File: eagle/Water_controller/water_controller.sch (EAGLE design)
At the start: 50 parts, among them IC1 MAX3232CSE, J1 J12MM, J2 J12MM, J3 J12MM, Q1 IRF740, T1 BT138-V, T2 BT138-V, T3 BT138-V

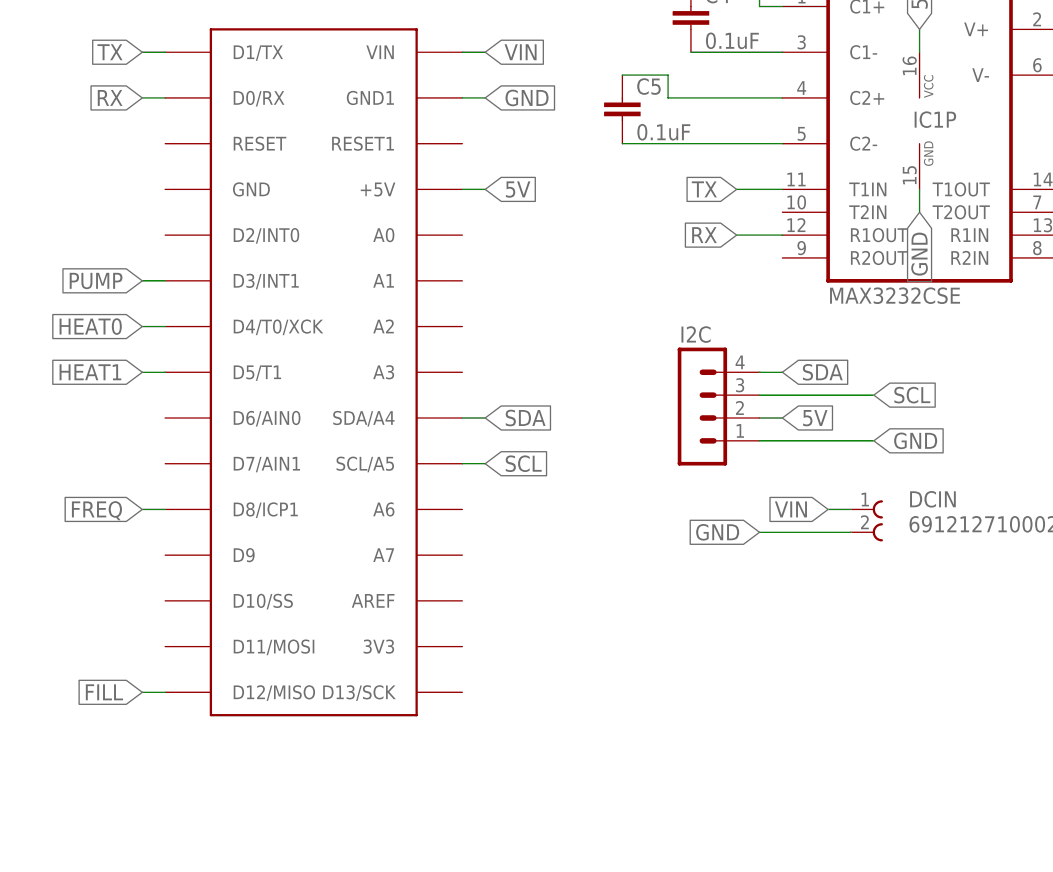
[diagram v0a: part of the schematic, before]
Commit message: Defined two more time periods: medium and fast, set state machine to run in medium tome perod, and separated USART, statemachine and logging, such that they are indipendent and USART and logging are not called within the state machine. Muche feedback needed and ALL code so far 8)
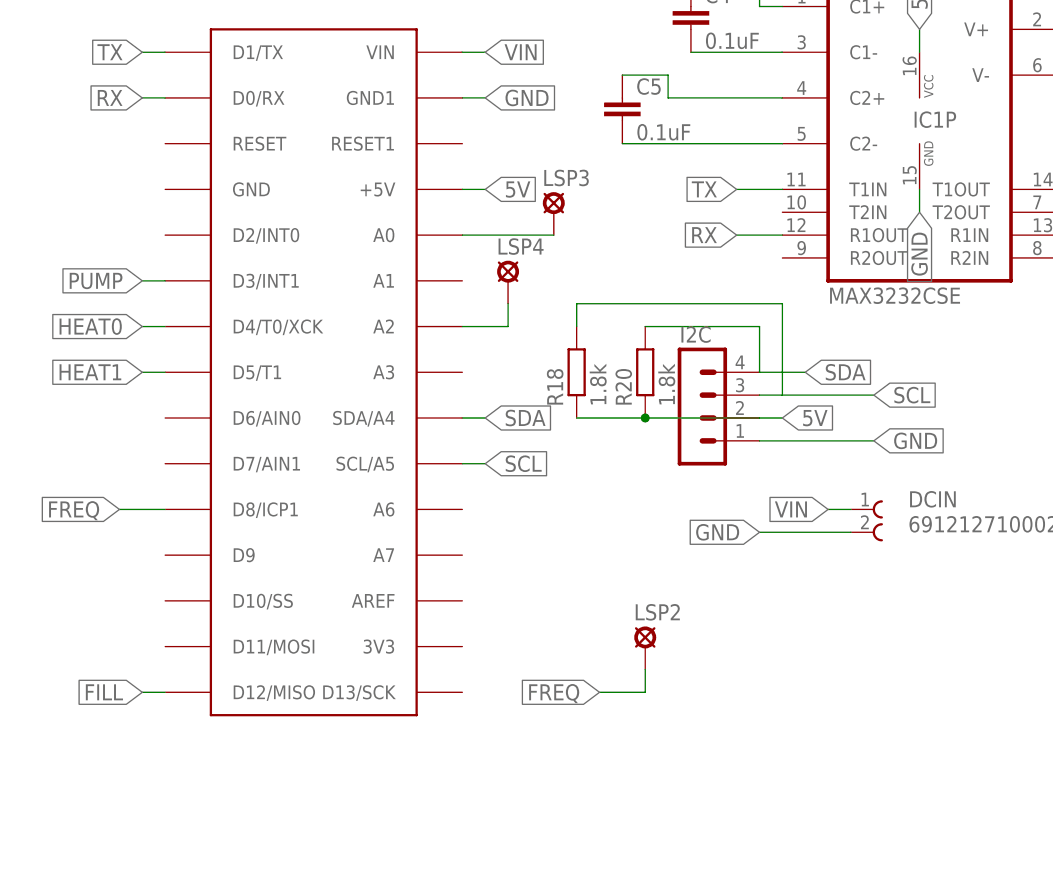
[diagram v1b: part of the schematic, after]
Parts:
- added LSP2, LSP3, LSP4: LSP11, solpad:LSP11
- added R18, R20: 1.8k, resistor:R-EU_R1206
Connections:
- new net N$33: LSP4.MP, U$1.A2
- new net N$34: LSP3.MP, U$1.A0
- net 5V: now also R18.1, R20.1
- net FREQ: now also LSP2.MP
- net SCL: now also R18.2
- net SDA: now also R20.2
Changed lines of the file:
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@@
 <grid distance="0.1" unitdist="inch" unit="inch" style="lines" multiple="1" display="no" altdistance="0.01" altunitdist="inch" altunit="inch"/>
 <layers>
-<layer number="1" name="Top" color="4" fill="1" visible="yes" active="no"/>
-<layer number="16" name="Bottom" color="1" fill="1" visible="yes" active="no"/>
-<layer number="17" name="Pads" color="2" fill="1" visible="yes" active="no"/>
-<layer number="18" name="Vias" color="2" fill="1" visible="yes" active="no"/>
-<layer number="19" name="Unrouted" color="6" fill="1" visible="yes" active="no"/>
-<layer number="20" name="Dimension" color="15" fill="1" visible="yes" active="no"/>
-<layer number="21" name="tPlace" color="7" fill="1" visible="yes" active="no"/>
-<layer number="22" name="bPlace" color="7" fill="1" visible="yes" active="no"/>
-<layer number="23" name="tOrigins" color="15" fill="1" visible="yes" active="no"/>
-<layer number="24" name="bOrigins" color="15" fill="1" visible="yes" active="no"/>
-<layer number="25" name="tNames" color="7" fill="1" visible="yes" active="no"/>
-<layer number="26" name="bNames" color="7" fill="1" visible="yes" active="no"/>
-<layer number="27" name="tValues" color="7" fill="1" visible="yes" active="no"/>
-<layer number="28" name="bValues" color="7" fill="1" visible="yes" active="no"/>
+<layer number="1" name="Top" color="4" fill="1" visible="no" active="no"/>
+<layer number="16" name="Bottom" color="1" fill="1" visible="no" active="no"/>
+<layer number="17" name="Pads" color="2" fill="1" visible="no" active="no"/>
+<layer number="18" name="Vias" color="2" fill="1" visible="no" active="no"/>
+<layer number="19" name="Unrouted" color="6" fill="1" visible="no" active="no"/>
+<layer number="20" name="Dimension" color="15" fill="1" visible="no" active="no"/>
+<layer number="21" name="tPlace" color="7" fill="1" visible="no" active="no"/>
+<layer number="22" name="bPlace" color="7" fill="1" visible="no" active="no"/>
+<layer number="23" name="tOrigins" color="15" fill="1" visible="no" active="no"/>
+<layer number="24" name="bOrigins" color="15" fill="1" visible="no" active="no"/>
+<layer number="25" name="tNames" color="7" fill="1" visible="no" active="no"/>
+<layer number="26" name="bNames" color="7" fill="1" visible="no" active="no"/>
+<layer number="27" name="tValues" color="7" fill="1" visible="no" active="no"/>
+<layer number="28" name="bValues" color="7" fill="1" visible="no" active="no"/>
 <layer number="29" name="tStop" color="7" fill="3" visible="no" active="no"/>
 <layer number="30" name="bStop" color="7" fill="6" visible="no" active="no"/>
@@
 <layer number="35" name="tGlue" color="7" fill="4" visible="no" active="no"/>
 <layer number="36" name="bGlue" color="7" fill="5" visible="no" active="no"/>
-<layer number="37" name="tTest" color="7" fill="1" visible="yes" active="no"/>
-<layer number="38" name="bTest" color="7" fill="1" visible="yes" active="no"/>
+<layer number="37" name="tTest" color="7" fill="1" visible="no" active="no"/>
+<layer number="38" name="bTest" color="7" fill="1" visible="no" active="no"/>
 <layer number="39" name="tKeepout" color="4" fill="11" visible="no" active="no"/>
 <layer number="40" name="bKeepout" color="1" fill="11" visible="no" active="no"/>
@@
 <layer number="44" name="Drills" color="7" fill="1" visible="no" active="no"/>
 <layer number="45" name="Holes" color="7" fill="1" visible="no" active="no"/>
-<layer number="46" name="Milling" color="3" fill="1" visible="yes" active="no"/>
-<layer number="47" name="Measures" color="7" fill="1" visible="yes" active="no"/>
-<layer number="48" name="Document" color="7" fill="1" visible="yes" active="no"/>
-<layer number="49" name="Reference" color="7" fill="1" visible="yes" active="no"/>
-<layer number="51" name="tDocu" color="7" fill="1" visible="yes" active="no"/>
-<layer number="52" name="bDocu" color="7" fill="1" visible="yes" active="no"/>
+<layer number="46" name="Milling" color="3" fill="1" visible="no" active="no"/>
+<layer number="47" name="Measures" color="7" fill="1" visible="no" active="no"/>
+<layer number="48" name="Document" color="7" fill="1" visible="no" active="no"/>
+<layer number="49" name="Reference" color="7" fill="1" visible="no" active="no"/>
+<layer number="51" name="tDocu" color="7" fill="1" visible="no" active="no"/>
+<layer number="52" name="bDocu" color="7" fill="1" visible="no" active="no"/>
 <layer number="91" name="Nets" color="2" fill="1" visible="yes" active="yes"/>
 <layer number="92" name="Busses" color="1" fill="1" visible="yes" active="yes"/>
@@
 <part name="J2" library="jumper" deviceset="J" device="12MM"/>
 <part name="J3" library="jumper" deviceset="J" device="12MM"/>
+<part name="R18" library="resistor" deviceset="R-EU_" device="R1206" value="1.8k"/>
+<part name="R20" library="resistor" deviceset="R-EU_" device="R1206" value="1.8k"/>
+<part name="LSP2" library="solpad" deviceset="LSP11" device=""/>
+<part name="LSP3" library="solpad" deviceset="LSP11" device=""/>
+<part name="LSP4" library="solpad" deviceset="LSP11" device=""/>
 </parts>
 <sheets>
@@
 <instance part="J2" gate="1" x="127" y="22.86"/>
 <instance part="J3" gate="1" x="127" y="-7.62"/>
+<instance part="R18" gate="G$1" x="-12.7" y="58.42" rot="R90"/>
+<instance part="R20" gate="G$1" x="-5.08" y="58.42" rot="R90"/>
+<instance part="LSP2" gate="1" x="-5.08" y="27.94"/>
+<instance part="LSP3" gate="1" x="-15.24" y="76.2"/>
+<instance part="LSP4" gate="1" x="-20.32" y="68.58"/>
 </instances>
 <busses>
@@
 <wire x1="7.62" y1="53.34" x2="10.16" y2="53.34" width="0.1524" layer="91"/>
 <label x="10.16" y="53.34" size="1.778" layer="95" xref="yes"/>
+<pinref part="R18" gate="G$1" pin="1"/>
+<wire x1="7.62" y1="53.34" x2="-5.08" y2="53.34" width="0.1524" layer="91"/>
+<pinref part="R20" gate="G$1" pin="1"/>
+<wire x1="-5.08" y1="53.34" x2="-12.7" y2="53.34" width="0.1524" layer="91"/>
+<junction x="-5.08" y="53.34"/>
 </segment>
 </net>
@@
 <segment>
 <pinref part="I2C" gate="1" pin="4"/>
-<wire x1="7.62" y1="58.42" x2="10.16" y2="58.42" width="0.1524" layer="91"/>
-<label x="10.16" y="58.42" size="1.778" layer="95" xref="yes"/>
+<wire x1="7.62" y1="58.42" x2="12.7" y2="58.42" width="0.1524" layer="91"/>
+<label x="12.7" y="58.42" size="1.778" layer="95" xref="yes"/>
+<wire x1="7.62" y1="58.42" x2="7.62" y2="63.5" width="0.1524" layer="91"/>
+<pinref part="R20" gate="G$1" pin="2"/>
+<wire x1="7.62" y1="63.5" x2="-5.08" y2="63.5" width="0.1524" layer="91"/>
 </segment>
 </net>
@@
 <segment>
 <pinref part="I2C" gate="1" pin="3"/>
-<wire x1="7.62" y1="55.88" x2="20.32" y2="55.88" width="0.1524" layer="91"/>
+<wire x1="7.62" y1="55.88" x2="10.16" y2="55.88" width="0.1524" layer="91"/>
 <label x="20.32" y="55.88" size="1.778" layer="95" xref="yes"/>
+<wire x1="10.16" y1="55.88" x2="20.32" y2="55.88" width="0.1524" layer="91"/>
+<wire x1="10.16" y1="55.88" x2="10.16" y2="66.04" width="0.1524" layer="91"/>
+<wire x1="10.16" y1="66.04" x2="-12.7" y2="66.04" width="0.1524" layer="91"/>
+<pinref part="R18" gate="G$1" pin="2"/>
+<wire x1="-12.7" y1="66.04" x2="-12.7" y2="63.5" width="0.1524" layer="91"/>
 </segment>
 </net>
@@
 <segment>
 <pinref part="U$1" gate="G$1" pin="D8/ICP1"/>
-<wire x1="-58.42" y1="43.18" x2="-60.96" y2="43.18" width="0.1524" layer="91"/>
-<label x="-60.96" y="43.18" size="1.778" layer="95" rot="R180" xref="yes"/>
+<wire x1="-58.42" y1="43.18" x2="-63.5" y2="43.18" width="0.1524" layer="91"/>
+<label x="-63.5" y="43.18" size="1.778" layer="95" rot="R180" xref="yes"/>
+</segment>
+<segment>
+<pinref part="LSP2" gate="1" pin="MP"/>
+<wire x1="-10.16" y1="22.86" x2="-5.08" y2="22.86" width="0.1524" layer="91"/>
+<wire x1="-5.08" y1="22.86" x2="-5.08" y2="25.4" width="0.1524" layer="91"/>
+<label x="-10.16" y="22.86" size="1.778" layer="95" rot="R180" xref="yes"/>
 </segment>
 </net>
@@
 </segment>
 </net>
+<net name="N$34" class="0">
+<segment>
+<pinref part="U$1" gate="G$1" pin="A0"/>
+<pinref part="LSP3" gate="1" pin="MP"/>
+<wire x1="-25.4" y1="73.66" x2="-15.24" y2="73.66" width="0.1524" layer="91"/>
+</segment>
+</net>
+<net name="N$33" class="0">
+<segment>
+<pinref part="U$1" gate="G$1" pin="A2"/>
+<pinref part="LSP4" gate="1" pin="MP"/>
+<wire x1="-25.4" y1="63.5" x2="-20.32" y2="63.5" width="0.1524" layer="91"/>
+<wire x1="-20.32" y1="63.5" x2="-20.32" y2="66.04" width="0.1524" layer="91"/>
+</segment>
+</net>

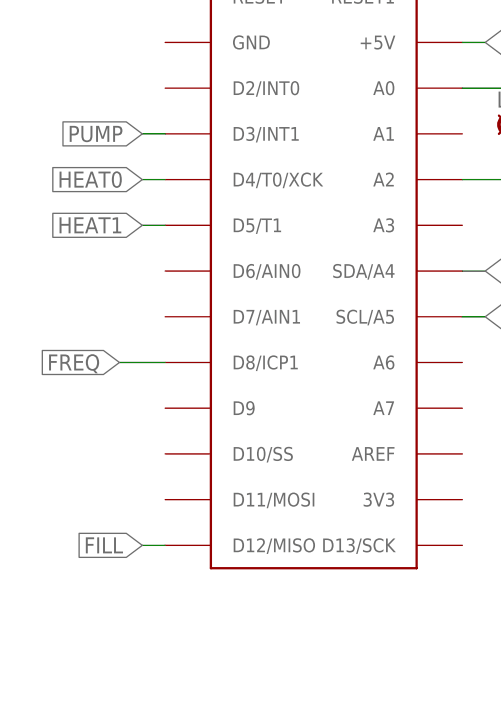
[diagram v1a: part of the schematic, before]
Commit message: Wow, a Version 1.0alpha! Should be a working system _when_ program is populated with values... still to be done. Lots and lots to do... oh so much for a project that was supposed to take two weeks. Next step is splitting into separate projects, then EDAC, Web interface and daemon. Pretty happy with it thus far it has to be said. If only the hardware would stop loosing legs and being annoying. The breakout board is for a chip that is just too tiny for words. Enjoy and go hard. Please pay note to the the use of bitwise operations in the state machine and check. logical operators may be more efficient.
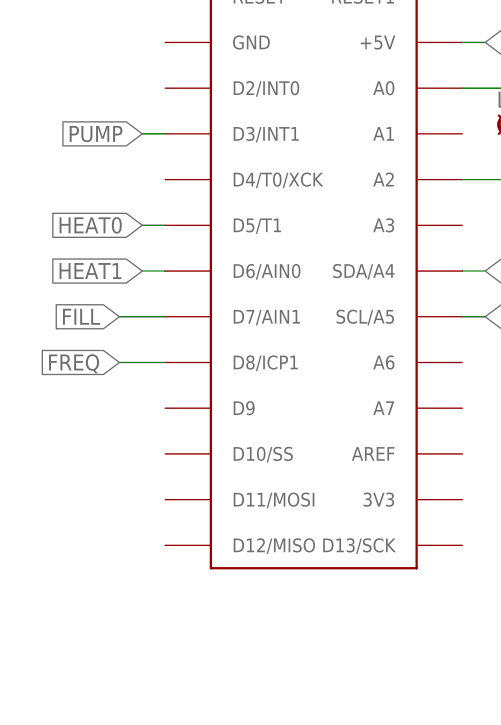
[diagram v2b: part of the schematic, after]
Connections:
- net FILL: now also U$1.D7/AIN1; no longer U$1.D12/MISO
- net HEAT0: now also U$1.D5/T1; no longer U$1.D4/T0/XCK
- net HEAT1: now also U$1.D6/AIN0; no longer U$1.D5/T1
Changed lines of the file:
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@@
 </segment>
 <segment>
-<pinref part="U$1" gate="G$1" pin="D5/T1"/>
-<wire x1="-58.42" y1="58.42" x2="-60.96" y2="58.42" width="0.1524" layer="91"/>
-<label x="-60.96" y="58.42" size="1.778" layer="95" rot="R180" xref="yes"/>
+<pinref part="U$1" gate="G$1" pin="D6/AIN0"/>
+<wire x1="-58.42" y1="53.34" x2="-60.96" y2="53.34" width="0.1524" layer="91"/>
+<label x="-60.96" y="53.34" size="1.778" layer="95" rot="MR0" xref="yes"/>
 </segment>
 </net>
@@
 </segment>
 <segment>
-<pinref part="U$1" gate="G$1" pin="D4/T0/XCK"/>
-<wire x1="-58.42" y1="63.5" x2="-60.96" y2="63.5" width="0.1524" layer="91"/>
-<label x="-60.96" y="63.5" size="1.778" layer="95" rot="R180" xref="yes"/>
+<pinref part="U$1" gate="G$1" pin="D5/T1"/>
+<wire x1="-58.42" y1="58.42" x2="-60.96" y2="58.42" width="0.1524" layer="91"/>
+<label x="-60.96" y="58.42" size="1.778" layer="95" rot="R180" xref="yes"/>
 </segment>
 </net>
@@
 </segment>
 <segment>
-<pinref part="U$1" gate="G$1" pin="D12/MISO"/>
-<wire x1="-58.42" y1="22.86" x2="-60.96" y2="22.86" width="0.1524" layer="91"/>
-<label x="-60.96" y="22.86" size="1.778" layer="95" rot="MR0" xref="yes"/>
-</segment>
-</net>
+<pinref part="U$1" gate="G$1" pin="D7/AIN1"/>
+<wire x1="-58.42" y1="48.26" x2="-63.5" y2="48.26" width="0.1524" layer="91"/>
+<label x="-63.5" y="48.26" size="1.778" layer="95" rot="MR0" xref="yes"/>
+</segment>
+</net>
